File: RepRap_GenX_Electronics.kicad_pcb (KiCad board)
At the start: 2 copper layers, 129.5 x 84.8 mm, 105 parts, among them J1 AXIS_X, J10 END_Y, J11 END_Z, J12 END_E0, J13 END_E1, J14 HEAT_E1, J15 TEMP_BED, J16 TEMP_E0, J17 TEMP_E1, J18 E1, J19 Conn_ARM_JTAG_SWD_10, J2 AXIS_Y, J20 12V_0, J21 12V_1, J22 FAN_0, J23 FAN_1, J3 MOT_PWR, J3_1 AXIS_Z1, J3_2 AXIS_Z2, J4 E0, J5 HEAT_PWR, J6 HEAT_E0, J7 HEAT_BED, J8 USB_B_Micro, J9 END_X, Q1 IRLIZ44N, Q2 IRLIZ44N, Q3 IRLIZ44N, Q4 DMN2300U, Q5 DMN2300U, SW1 SW_Push, U1 STM32F412RGTx, U2 ADP2303ARDZ-5.0, U3 USBLC6-2SC6, U4 TPS62160DSG

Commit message: Added ZVD and 5V breakout for external supply
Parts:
- added J24: Conn_02x02_Counter_Clockwise, Connector_PinHeader_2.54mm:PinHeader_2x02_P2.54mm_Vertical, F.Cu at (162.6, 63.5)
- added Q6: DMMT5401-7(A), Package_SO:SC-74-6_1.5x2.9mm_P0.95mm, F.Cu at (174.0, 99.8)
- added Q7: DMG2305UX, Package_TO_SOT_SMD:SOT-23, F.Cu at (169.7, 100.1)
- added R19: 10K, Resistor_SMD:R_0603_1608Metric, F.Cu at (174.0, 97.3)
- added R4: 10K, Resistor_SMD:R_0603_1608Metric, F.Cu at (174.0, 102.4)
- JP1: footprint Jumper:SolderJumper-2_P1.3mm_Open_TrianglePad1.0x1.5mm -> Connector_PinHeader_2.54mm:PinHeader_1x02_P2.54mm_Vertical
- moved G1 77.2 mm to (91.9, 93.5)
- moved JP1 25.9 mm to (126.7, 62.5)
- moved R3 24.5 mm to (126.7, 59.7), turned to 0 degrees
- moved R6 12.5 mm to (159.8, 93.9), turned to 0 degrees
- moved C29 10.7 mm to (159.8, 95.5), turned to 0 degrees
- moved L3 10.0 mm to (158.2, 98.6), turned to 270 degrees
- moved R7 9.33 mm to (163.1, 94.7), turned to 0 degrees
- moved R5 6.60 mm to (160.5, 99.3), turned to 270 degrees
- moved U4 6.48 mm to (163.1, 96.9), turned to 180 degrees
- moved C5 4.89 mm to (165.9, 97.8), turned to 270 degrees
- moved C18 2.57 mm to (163.1, 100.7), turned to 0 degrees
- moved L1 0.28 mm to (84.1, 60.2)
- moved J15 0.13 mm to (80.0, 66.3)
- moved J16 0.13 mm to (80.0, 76.7)
- moved J17 0.13 mm to (80.0, 87.1)
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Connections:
- C13 pad 1: Net-(C13-Pad1) -> GND
- C13 pad 2: GND -> Net-(C13-Pad2)
- C17 pad 2: +5V -> ZVD_5V
- C5 pad 1: +5V -> ZVD_5V
- J8 pad 1: +5V -> ZVD_5V
- U1 pad 30: Net-(C13-Pad1) -> Net-(C13-Pad2)
- U3 pad 5: +5V -> ZVD_5V
- U4 pad 2: +5V -> ZVD_5V
- U4 pad 3: +5V -> ZVD_5V
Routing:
- net ZVD_5V: track 0.00 -> 87.4 mm, vias 0 -> 2
- net +5V: track 109.3 -> 38.2 mm, vias 4 -> 2
- net Net-(JP1-Pad2): track 6.37 -> 39.5 mm
- net GND: track 943.0 -> 914.5 mm, vias 16 -> 17
- net VDD: track 337.7 -> 318.4 mm, vias 5 -> 6
- net V_MOT: track 318.4 -> 303.4 mm, vias 2 -> 1
- net Net-(Q6-Pad1): track 0.00 -> 4.78 mm
- net Net-(Q6-Pad4): track 0.00 -> 4.03 mm
- net Net-(C13-Pad2): track 0.00 -> 3.54 mm
- net Net-(C13-Pad1): track 3.54 -> 0.00 mm
- net /DIR_E1: track 77.5 -> 75.1 mm
- net /EN_E1: track 54.5 -> 52.3 mm
- net /STEP_E1: track 73.7 -> 71.5 mm
- net /CS_E1: track 64.9 -> 62.7 mm
- net /SPI_MOSI: track 104.4 -> 102.2 mm
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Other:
- board text added: "+5V"
- board text added: "GND"

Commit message: Added totem pole drivers for MOSFETs and split main schematic
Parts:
- removed C25, C26, C27, C28: 100nF, Capacitor_SMD:C_0402_1005Metric
- added C16: 100nF 6.3V, Capacitor_SMD:C_0402_1005Metric, F.Cu at (109.2, 106.7)
- added C2: 100nF 25V, Capacitor_SMD:C_0402_1005Metric, F.Cu at (91.4, 121.9)
- added C7: 100nF 6.3V, Capacitor_SMD:C_0402_1005Metric, F.Cu at (91.4, 106.7)
- added C8: 100nF 25V, Capacitor_SMD:C_0402_1005Metric, F.Cu at (109.2, 121.9)
- added D10: LG R971, LED_SMD:LED_0805_2012Metric_Castellated, F.Cu at (165.6, 106.4)
- added D11: LG R971, LED_SMD:LED_0805_2012Metric_Castellated, F.Cu at (148.6, 95.0)
- added D12: PMEG1020EH, Diode_SMD:D_SOD-123F, F.Cu at (170.4, 63.8)
- added D13: PMEG1020EH, Diode_SMD:D_SOD-123F, F.Cu at (170.4, 76.5)
- added D14: PMEG1020EH, Diode_SMD:D_SOD-123F, F.Cu at (170.4, 89.7)
- added D15: LS R976, LED_SMD:LED_0805_2012Metric_Castellated, F.Cu at (183.9, 67.6)
- added D16: LS R976, LED_SMD:LED_0805_2012Metric_Castellated, F.Cu at (183.9, 79.1)
- added D17: LS R976, LED_SMD:LED_0805_2012Metric_Castellated, F.Cu at (183.9, 90.7)
- added D18: SS14, Diode_SMD:D_SMA, F.Cu at (188.2, 69.9)
- added D19: SS14, Diode_SMD:D_SMA, F.Cu at (188.2, 81.4)
- added D20: SS14, Diode_SMD:D_SMA, F.Cu at (188.2, 93.0)
- added Q10: BCX56, Package_TO_SOT_SMD:SOT-89-3, F.Cu at (165.6, 62.2)
- added Q11: BCX51, Package_TO_SOT_SMD:SOT-89-3, F.Cu at (165.6, 67.6)
- added Q12: BCX56, Package_TO_SOT_SMD:SOT-89-3, F.Cu at (165.6, 75.2)
- added Q13: BCX51, Package_TO_SOT_SMD:SOT-89-3, F.Cu at (165.6, 80.5)
- added Q14: BCX56, Package_TO_SOT_SMD:SOT-89-3, F.Cu at (165.6, 88.1)
- added Q15: BCX51, Package_TO_SOT_SMD:SOT-89-3, F.Cu at (165.6, 93.5)
- added Q16: IRLIZ44N, Package_TO_SOT_THT:TO-220F-3_Vertical, F.Cu at (178.1, 65.3)
- added Q17: IRLIZ44N, Package_TO_SOT_THT:TO-220F-3_Vertical, F.Cu at (178.1, 76.8)
- added Q18: IRLIZ44N, Package_TO_SOT_THT:TO-220F-3_Vertical, F.Cu at (178.1, 88.4)
- added Q8: DMMT5401-7(A), Package_SO:SC-74-6_1.5x2.9mm_P0.95mm, F.Cu at (137.7, 70.9)
- added Q9: DMG2305UX, Package_TO_SOT_SMD:SOT-23, F.Cu at (137.7, 75.2)
- added R20: 150 0.125W, Resistor_SMD:R_0603_1608Metric, F.Cu at (166.4, 103.6)
- added R21: 56 0.125W, Resistor_SMD:R_0603_1608Metric, F.Cu at (148.6, 98.6)
- added R22: 10K, Resistor_SMD:R_0603_1608Metric, F.Cu at (140.2, 70.9)
- added R23: 10K, Resistor_SMD:R_0603_1608Metric, F.Cu at (135.1, 70.9)
- added R24: 10, Resistor_SMD:R_0805_2012Metric, F.Cu at (170.4, 61.5)
- added R25: 10, Resistor_SMD:R_0805_2012Metric, F.Cu at (170.4, 74.2)
- added R26: 10, Resistor_SMD:R_0805_2012Metric, F.Cu at (170.4, 87.4)
- added R27: 1.2K >0.5W, Resistor_SMD:R_2010_5025Metric, F.Cu at (185.8, 64.5)
- added R28: 1.2K >0.5W, Resistor_SMD:R_2010_5025Metric, F.Cu at (185.8, 76.1)
- added R29: 1.2K >0.5W, Resistor_SMD:R_2010_5025Metric, F.Cu at (185.8, 87.6)
- C1: value 10uF -> 10uF 35V
- C10, C11, C12, C20, C22, C24, C3, C30, C6, C9: value 100nF -> 100nF 6.3V
- C15, C17: value 1uF -> 1uF 6.3V; footprint Capacitor_SMD:C_0805_2012Metric -> Capacitor_SMD:C_0402_1005Metric
- C18: footprint Capacitor_SMD:C_0805_2012Metric -> Capacitor_SMD:C_0603_1608Metric
- C19, C21, C23: value 100nF -> 100nF 25V
- C29: footprint Capacitor_SMD:C_0402_1005Metric -> Capacitor_SMD:C_0201_0603Metric
- C4: value 47uF -> 47uF 6.3V X5R
- C5: value 10uF -> 10uF 6.3V
- D2, D3, D4: value LED -> BZX84Cxx; footprint LED_SMD:LED_0603_1608Metric -> Diode_SMD:D_SOT-23_ANK
- D5, D6: value D -> SS14
- D7, D8, D9: value D -> BZX84Cxx; footprint Diode_SMD:D_SMA -> Diode_SMD:D_SOT-23_ANK
- J1: value AXIS_X -> END_X; footprint Connector_Molex:Molex_KK-254_AE-6410-04A_1x04_P2.54mm_Vertical -> Connector_Molex:Molex_KK-254_AE-6410-03A_1x03_P2.54mm_Vertical
- J10: value END_Y -> FAN_1; footprint Connector_Molex:Molex_KK-254_AE-6410-03A_1x03_P2.54mm_Vertical -> Connector_Molex:Molex_KK-254_AE-6410-02A_1x02_P2.54mm_Vertical
- J11: value END_Z -> TEMP_BED; footprint Connector_Molex:Molex_KK-254_AE-6410-03A_1x03_P2.54mm_Vertical -> Connector_Molex:Molex_KK-254_AE-6410-02A_1x02_P2.54mm_Vertical
- J12: value END_E0 -> TEMP_E0; footprint Connector_Molex:Molex_KK-254_AE-6410-03A_1x03_P2.54mm_Vertical -> Connector_Molex:Molex_KK-254_AE-6410-02A_1x02_P2.54mm_Vertical
- J13: value END_E1 -> TEMP_E1; footprint Connector_Molex:Molex_KK-254_AE-6410-03A_1x03_P2.54mm_Vertical -> Connector_Molex:Molex_KK-254_AE-6410-02A_1x02_P2.54mm_Vertical
- J14: value HEAT_E1 -> AXIS_X; footprint Connector_Molex:Molex_KK-396_A-41791-0002_1x02_P3.96mm_Vertical -> Connector_Molex:Molex_KK-254_AE-6410-04A_1x04_P2.54mm_Vertical
- J15: value TEMP_BED -> AXIS_Y; footprint Connector_Molex:Molex_KK-254_AE-6410-02A_1x02_P2.54mm_Vertical -> Connector_Molex:Molex_KK-254_AE-6410-04A_1x04_P2.54mm_Vertical
- J16: value TEMP_E0 -> E0; footprint Connector_Molex:Molex_KK-254_AE-6410-02A_1x02_P2.54mm_Vertical -> Connector_Molex:Molex_KK-254_AE-6410-04A_1x04_P2.54mm_Vertical
- J17: value TEMP_E1 -> E1; footprint Connector_Molex:Molex_KK-254_AE-6410-02A_1x02_P2.54mm_Vertical -> Connector_Molex:Molex_KK-254_AE-6410-04A_1x04_P2.54mm_Vertical
- J18: value E1 -> HEAT_BED; footprint Connector_Molex:Molex_KK-254_AE-6410-04A_1x04_P2.54mm_Vertical -> Connector_Molex:Molex_KK-396_A-41791-0002_1x02_P3.96mm_Vertical
- J2: value AXIS_Y -> END_Y; footprint Connector_Molex:Molex_KK-254_AE-6410-04A_1x04_P2.54mm_Vertical -> Connector_Molex:Molex_KK-254_AE-6410-03A_1x03_P2.54mm_Vertical
- J22: value FAN_0 -> HEAT_E0; footprint Connector_Molex:Molex_KK-254_AE-6410-02A_1x02_P2.54mm_Vertical -> Connector_Molex:Molex_KK-396_A-41791-0002_1x02_P3.96mm_Vertical
- J23: value FAN_1 -> HEAT_E1; footprint Connector_Molex:Molex_KK-254_AE-6410-02A_1x02_P2.54mm_Vertical -> Connector_Molex:Molex_KK-396_A-41791-0002_1x02_P3.96mm_Vertical
- J4: value E0 -> END_Z; footprint Connector_Molex:Molex_KK-254_AE-6410-04A_1x04_P2.54mm_Vertical -> Connector_Molex:Molex_KK-254_AE-6410-03A_1x03_P2.54mm_Vertical
- J6: value HEAT_E0 -> END_E0; footprint Connector_Molex:Molex_KK-396_A-41791-0002_1x02_P3.96mm_Vertical -> Connector_Molex:Molex_KK-254_AE-6410-03A_1x03_P2.54mm_Vertical
- J7: value HEAT_BED -> END_E1; footprint Connector_Molex:Molex_KK-396_A-41791-0002_1x02_P3.96mm_Vertical -> Connector_Molex:Molex_KK-254_AE-6410-03A_1x03_P2.54mm_Vertical
- J9: value END_X -> FAN_0; footprint Connector_Molex:Molex_KK-254_AE-6410-03A_1x03_P2.54mm_Vertical -> Connector_Molex:Molex_KK-254_AE-6410-02A_1x02_P2.54mm_Vertical
- Q1, Q2: value IRLIZ44N -> DMN3713U; footprint Package_TO_SOT_THT:TO-220F-3_Vertical -> Package_TO_SOT_SMD:SOT-23
- Q3: value IRLIZ44N -> BC817; footprint Package_TO_SOT_THT:TO-220F-3_Vertical -> Package_TO_SOT_SMD:SOT-23
- Q4, Q5: value DMN2300U -> BC817
- R11, R12, R13: value 4.7K -> 1K
- R14, R15: value 2.2K -> 1K
- R16: value 2.2K -> 4.7K 1%; footprint Resistor_SMD:R_0805_2012Metric -> Resistor_SMD:R_0603_1608Metric
- R17, R18: value 1K -> 4.7K 1%; footprint Resistor_SMD:R_0805_2012Metric -> Resistor_SMD:R_0603_1608Metric
- moved J14 117.0 mm to (86.4, 130.8), turned to 180 degrees
- moved R16 106.5 mm to (78.9, 70.9), turned to 180 degrees
- moved J7 105.1 mm to (90.7, 59.9)
- moved J6 98.8 mm to (98.3, 59.9)
- moved J17 88.9 mm to (157.5, 130.8)
- moved R13 88.0 mm to (161.3, 61.2), turned to 0 degrees
- moved R18 81.6 mm to (78.7, 91.7)
- moved J16 80.6 mm to (139.7, 130.8)
- moved R12 79.4 mm to (157.7, 88.9)
- moved R11 79.2 mm to (157.7, 75.9)
- moved J1 78.9 mm to (121.2, 59.9), turned to 270 degrees
- moved J4 78.5 mm to (105.9, 59.9), turned to 270 degrees
- moved J18 75.4 mm to (195.6, 65.8), turned to 270 degrees
- moved D5 75.3 mm to (117.9, 95.2)
- moved J2 71.5 mm to (113.5, 59.9), turned to 270 degrees
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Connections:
- C17 pad 2: ZVD_5V -> USB_5V
- C22 pad 1: VDD -> GND
- C22 pad 2: GND -> VDD
- C24 pad 1: VDD -> GND
- C24 pad 2: GND -> VDD
- D2 pad 2: Net-(D2-Pad2) -> GND
- D3 pad 2: Net-(D3-Pad2) -> GND
- D4 pad 2: Net-(D4-Pad2) -> GND
- D5 pad 1: V_HEAT -> V_MOT
- D5 pad 2: Net-(D2-Pad1) -> Net-(D5-Pad2)
- D6 pad 1: V_HEAT -> V_MOT
- D6 pad 2: Net-(D3-Pad1) -> Net-(D6-Pad2)
- D7 pad 1: V_HEAT -> MOS_HBED
- D7 pad 2: Net-(D4-Pad1) -> GND
- D8 pad 1: V_MOT -> MOS_HE0
- D8 pad 2: Net-(D8-Pad2) -> GND
- D9 pad 1: V_MOT -> MOS_HE1
- D9 pad 2: Net-(D9-Pad2) -> GND
- J1 pad 1: Net-(A1-Pad11) -> VDD
- J1 pad 2: Net-(A1-Pad12) -> GND
- J1 pad 3: Net-(A1-Pad13) -> /END_X
- J10 pad 1: VDD -> V_MOT
- J10 pad 2: GND -> Net-(D6-Pad2)
- J11 pad 1: VDD -> /TEMP_BED
- J12 pad 1: VDD -> /TEMP_E0
- J13 pad 1: VDD -> /TEMP_E1
- J14 pad 1: V_HEAT -> Net-(A1-Pad11)
- J14 pad 2: Net-(D4-Pad1) -> Net-(A1-Pad12)
- J15 pad 1: /TEMP_BED -> Net-(A2-Pad11)
- J15 pad 2: GND -> Net-(A2-Pad12)
- J16 pad 1: /TEMP_E0 -> Net-(A4-Pad11)
- J16 pad 2: GND -> Net-(A4-Pad12)
- J17 pad 1: /TEMP_E1 -> Net-(A5-Pad11)
- J17 pad 2: GND -> Net-(A5-Pad12)
- J18 pad 1: Net-(A5-Pad11) -> V_HEAT
- J18 pad 2: Net-(A5-Pad12) -> Net-(D15-Pad1)
- J2 pad 1: Net-(A2-Pad11) -> VDD
- J2 pad 2: Net-(A2-Pad12) -> GND
- J2 pad 3: Net-(A2-Pad13) -> /END_Y
- J22 pad 1: V_MOT -> V_HEAT
- J22 pad 2: Net-(D8-Pad2) -> Net-(D16-Pad1)
- J23 pad 1: V_MOT -> V_HEAT
- J23 pad 2: Net-(D9-Pad2) -> Net-(D17-Pad1)
- J4 pad 1: Net-(A4-Pad11) -> VDD
- J4 pad 2: Net-(A4-Pad12) -> GND
- J4 pad 3: Net-(A4-Pad13) -> /END_Z
- J6 pad 1: V_HEAT -> VDD
- J6 pad 2: Net-(D3-Pad1) -> GND
- J7 pad 1: V_HEAT -> VDD
- J7 pad 2: Net-(D2-Pad1) -> GND
- J8 pad 1: ZVD_5V -> USB_5V
- J9 pad 1: VDD -> V_MOT
- J9 pad 2: GND -> Net-(D5-Pad2)
- Q1 pad 2: Net-(D2-Pad1) -> GND
- Q1 pad 3: GND -> Net-(D5-Pad2)
- Q2 pad 2: Net-(D3-Pad1) -> GND
- Q2 pad 3: GND -> Net-(D6-Pad2)
- Q3 pad 2: Net-(D4-Pad1) -> GND
- Q3 pad 3: GND -> Net-(D2-Pad1)
- Q4 pad 3: Net-(D8-Pad2) -> Net-(D3-Pad1)
- Q5 pad 3: Net-(D9-Pad2) -> Net-(D4-Pad1)
- R10 pad 2: /PWMH_E1 -> /PWMH_BED
- R11 pad 1: /TEMP_BED -> Net-(Q4-Pad1)
- R11 pad 2: VDDA -> /PWMH_E0
- R12 pad 1: /TEMP_E0 -> Net-(Q5-Pad1)
- R12 pad 2: VDDA -> /PWMH_E1
- R13 pad 1: /TEMP_E1 -> V_HEAT
- R13 pad 2: VDDA -> Net-(D2-Pad1)
- R14 pad 1: Net-(D2-Pad2) -> V_HEAT
- R14 pad 2: V_HEAT -> Net-(D3-Pad1)
- R15 pad 1: Net-(D3-Pad2) -> V_HEAT
- R15 pad 2: V_HEAT -> Net-(D4-Pad1)
- R16 pad 1: Net-(D4-Pad2) -> /TEMP_BED
- R16 pad 2: V_HEAT -> VDDA
- R17 pad 1: Net-(Q4-Pad1) -> /TEMP_E0
- R17 pad 2: /PWM_FAN0 -> VDDA
- R18 pad 1: Net-(Q5-Pad1) -> /TEMP_E1
- R18 pad 2: /PWM_FAN1 -> VDDA
- R8 pad 2: /PWMH_BED -> /PWM_FAN0
- R9 pad 2: /PWMH_E0 -> /PWM_FAN1
- U1 pad 34: /EN_E0 -> /PWM_FAN1
- U1 pad 35: /CS_E0 -> /PWM_FAN0
- U1 pad 36: /STEP_E0 -> /EN_E0
- U1 pad 37: /DIR_E0 -> /CS_E0
- U1 pad 38: /EN_E1 -> /STEP_E0
- U1 pad 39: /CS_E1 -> /DIR_E0
- U1 pad 40: /STEP_E1 -> /EN_E1
- U1 pad 41: /DIR_E1 -> /CS_E1
- U1 pad 42: /PWM_FAN0 -> /STEP_E1
- U1 pad 43: /PWM_FAN1 -> /DIR_E1
- U3 pad 5: ZVD_5V -> USB_5V
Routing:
- net V_HEAT: track 94.9 -> 204.9 mm
- net +5V: track 38.2 -> 101.7 mm, vias 2 -> 3
- net GND: track 914.5 -> 976.7 mm, vias 17 -> 14
- net /PWM_FAN0: track 34.9 -> 64.7 mm
- net USB_5V: track 0.00 -> 22.9 mm
- net Net-(D15-Pad1): track 0.00 -> 22.3 mm
- net Net-(D16-Pad1): track 0.00 -> 22.3 mm
- net Net-(D17-Pad1): track 0.00 -> 22.3 mm
- net /PWMH_E1: track 80.3 -> 59.7 mm
- net ZVD_5V: track 87.4 -> 67.6 mm, vias 2 -> 1
- net /PWMH_E0: track 71.0 -> 53.5 mm
- net MOS_HBED: track 0.00 -> 13.4 mm
- net /EN_E0: track 49.2 -> 62.3 mm
- net MOS_HE0: track 0.00 -> 12.9 mm
- net MOS_HE1: track 0.00 -> 12.2 mm
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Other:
- net class Default: clearance 0.2 -> 0.1524
- net class HEAT_PWR: clearance 0.2 -> 0.1524
- net class V_HEAT: clearance 0.2 -> 0.1524
- net class V_MOT: clearance 0.2 -> 0.1524
- net class V_PWR: clearance 0.2 -> 0.1524
- net class V_STEP: clearance 0.2 -> 0.1524
- rule trace_clearance: 0.2 -> 0.1524
- rule trace_min: 0.2 -> 0.1524

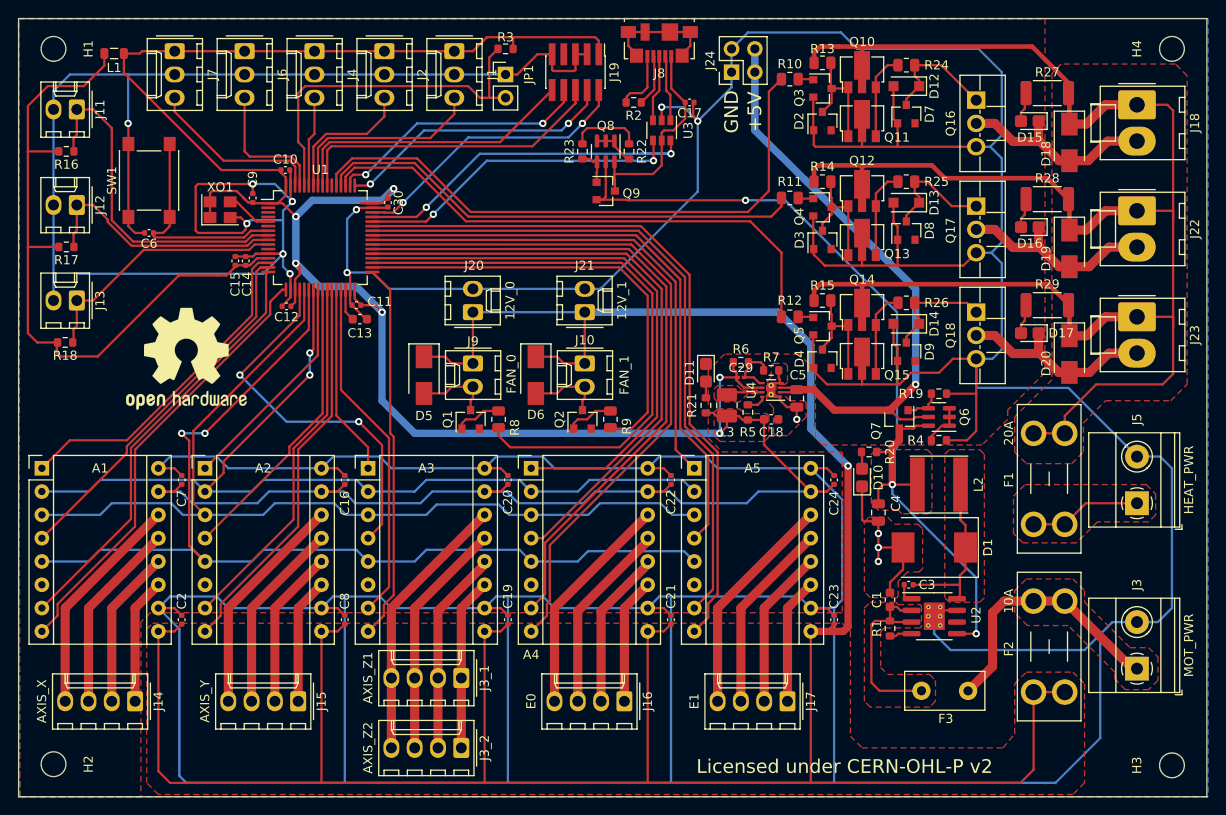
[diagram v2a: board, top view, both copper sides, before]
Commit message: Added I2C and 3.3v breakout for expansion port
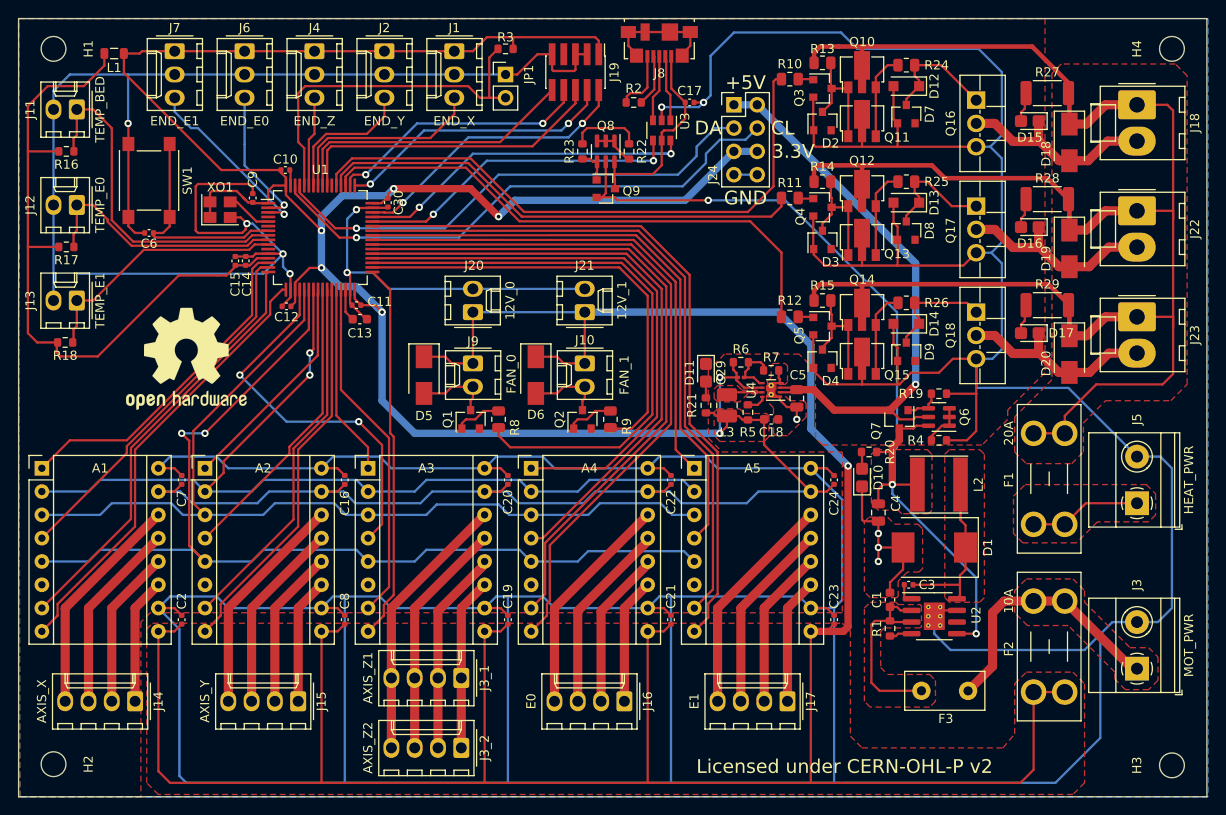
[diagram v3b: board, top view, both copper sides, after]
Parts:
- J24: value Conn_02x02_Counter_Clockwise -> Conn_02x04_Odd_Even; footprint Connector_PinHeader_2.54mm:PinHeader_2x02_P2.54mm_Vertical -> Connector_PinHeader_2.54mm:PinHeader_2x04_P2.54mm_Vertical
- moved J24 3.57 mm to (151.6, 65.8), turned to 0 degrees
- moved Q9 0.25 mm to (137.7, 74.9)
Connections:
- J24 pad 1: GND -> ZVD_5V
- J24 pad 2: GND -> ZVD_5V
- J24 pad 3: ZVD_5V -> I2C1_SDA
- J24 pad 4: ZVD_5V -> I2C1_SCL
- U1 pad 2: (no net) -> /END_E0
- U1 pad 3: (no net) -> /END_E1
- U1 pad 61: /END_E0 -> I2C1_SDA
- U1 pad 62: /END_E1 -> I2C1_SCL
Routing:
- net I2C1_SCL: track 0.00 -> 58.8 mm, vias 0 -> 1
- net I2C1_SDA: track 0.00 -> 54.8 mm, vias 0 -> 1
- net VDD: track 311.1 -> 352.3 mm, vias 6 -> 7
- net GND: track 976.7 -> 939.4 mm, vias 14 -> 12
- net ZVD_5V: track 67.6 -> 63.9 mm
- net /END_E1: track 19.2 -> 19.9 mm, vias 0 -> 1
- net /END_E0: track 14.7 -> 15.3 mm, vias 0 -> 1
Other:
- board text added: "3.3V"
- board text added: "CL"
- board text added: "DA"
